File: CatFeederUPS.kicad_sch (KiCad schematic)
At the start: 18 parts, among them J1 JST-PH-2, J2 FEEDER-OUT, U2 BQ24079RGT, U3 TPS61235PRWLR

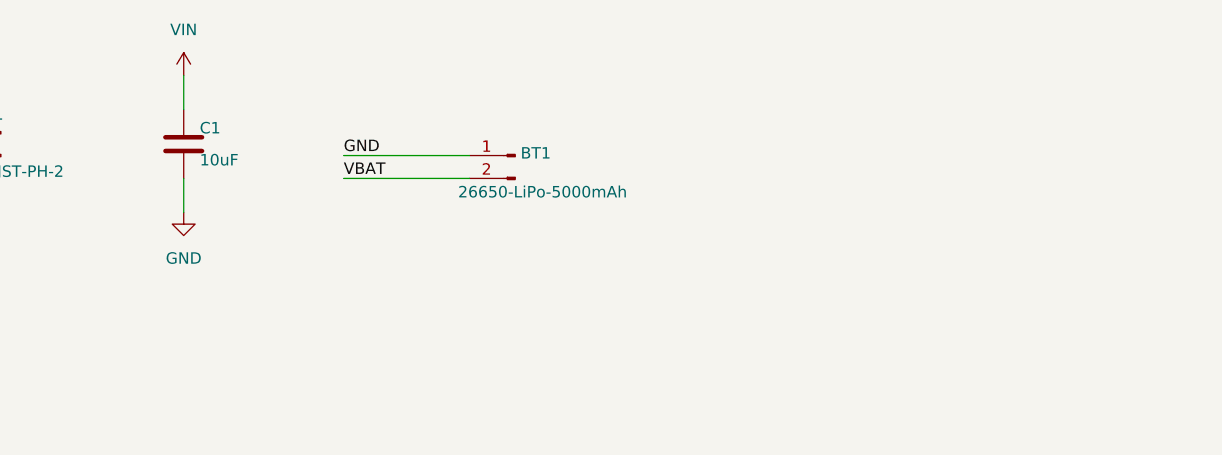
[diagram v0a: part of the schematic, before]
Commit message: Basic layout done, but...
There are a lot of problems with the TPW21635P footprint. It's got a
gigantic  pad 2 (SW) that's a weird T-shape, and both the SnapEDA and
Ultra Librarian footprints represent this as a "polygon" overlaid over
a "pad", which causes DRC to complain bitterly about both electrical
overlap and soldermask overlap, which I cannot fix with board setup,
design rules exceptions etc. etc.

So I had to resort to editing the footprint: I selected the pad, clicked
"edit pad  as geometry shapes" or something in the right-click context
menu, selected both the pad and the polygon, and hit ctrl-e, then saved
it back to the library.

This has fixed the DRC complaints, hopefully I haven't banjaxed it...
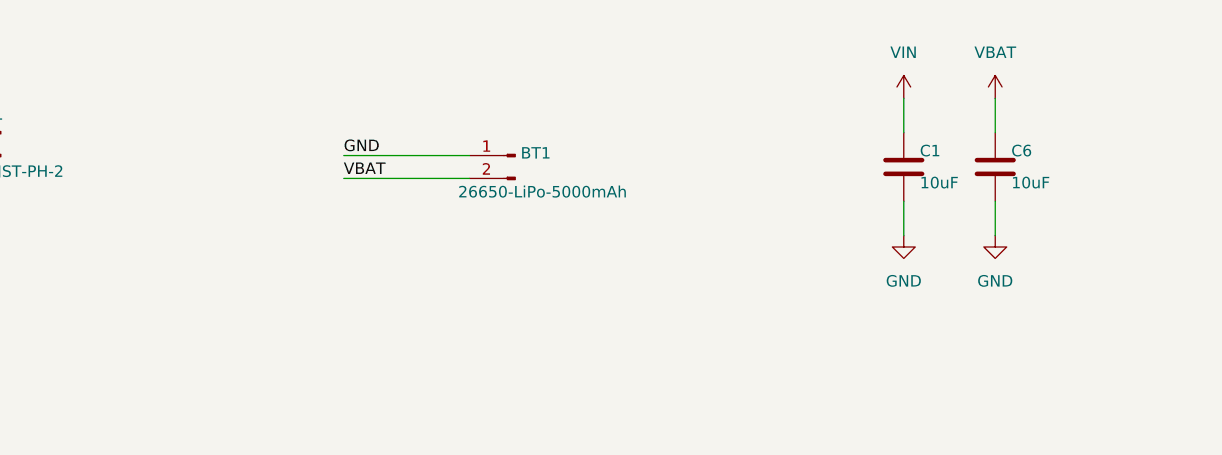
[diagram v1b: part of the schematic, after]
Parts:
- added C6: 10uF, Capacitor_SMD:C_0402_1005Metric, symbol Device:C
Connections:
- net GND: now also C6.2
- net VBAT: now also C6.1
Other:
- moved on the sheet: C1

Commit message: fix LCSC part numbers, and the goddam TPS61235 footprint **again**
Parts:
- BT1, J2: now left out of the parts list
- D2: LCSC C2286 -> C12624
- J1: LCSC C173752 -> (none); now left out of the parts list
- L1: LCSC C408536 -> C695604
- R4, R6: LCSC C11702 -> C114759
- R5: LCSC C11702 -> C60490
- R7: LCSC C11702 -> C3016052
- R8: LCSC C11702 -> C453521
- U2: LCSC (none) -> C140287
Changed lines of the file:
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@@
 			)
 		)
-		(property "LCSC" "C11702"
+		(property "LCSC" "C114759"
 			(at 119.38 105.41 0)
 			(hide yes)
@@
 		(body_style 1)
 		(exclude_from_sim no)
-		(in_bom yes)
+		(in_bom no)
 		(on_board yes)
 		(in_pos_files yes)
@@
 			)
 		)
-		(property "LCSC" "C173752"
-			(at 41.91 43.18 0)
-			(hide yes)
-			(show_name no)
-			(do_not_autoplace no)
-			(effects
-				(font
-					(size 1.27 1.27)
-				)
-			)
-		)
 		(pin "2"
 		)
@@
 			)
 		)
+		(property "LCSC" "C140287"
+			(at 57.15 107.95 0)
+			(hide yes)
+			(show_name no)
+			(do_not_autoplace no)
+			(effects
+				(font
+					(size 1.27 1.27)
+				)
+			)
+		)
 		(pin "8"
 		)
@@
 			)
 		)
-		(property "LCSC" "C11702"
+		(property "LCSC" "C60490"
 			(at 92.71 124.46 0)
 			(hide yes)
@@
 		(body_style 1)
 		(exclude_from_sim no)
-		(in_bom yes)
+		(in_bom no)
 		(on_board yes)
 		(in_pos_files yes)
@@
 			)
 		)
-		(property "LCSC" "C408536"
+		(property "LCSC" "C695604"
 			(at 194.31 83.82 0)
 			(hide yes)
@@
 		(body_style 1)
 		(exclude_from_sim no)
-		(in_bom yes)
+		(in_bom no)
 		(on_board yes)
 		(in_pos_files yes)
@@
 			)
 		)
-		(property "LCSC" "C11702"
+		(property "LCSC" "C3016052"
 			(at 29.21 121.92 0)
 			(hide yes)
@@
 			)
 		)
-		(property "LCSC" "C11702"
+		(property "LCSC" "C114759"
 			(at 104.14 105.41 0)
 			(hide yes)
@@
 			)
 		)
-		(property "LCSC" "C2286"
+		(property "LCSC" "C12624"
 			(at 119.38 93.98 0)
 			(hide yes)
@@
 			)
 		)
-		(property "LCSC" "C11702"
+		(property "LCSC" "C453521"
 			(at 40.64 121.92 0)
 			(hide yes)

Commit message: a couple more component swaps, and away into production we go!
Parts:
- D1: LCSC C2286 -> C130719
- D2: LCSC C12624 -> C74338
- R8: LCSC C453521 -> C67014
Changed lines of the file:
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@@
 			)
 		)
-		(property "LCSC" "C2286"
+		(property "LCSC" "C130719"
 			(at 104.14 93.98 0)
 			(hide yes)
@@
 			)
 		)
-		(property "LCSC" "C12624"
+		(property "LCSC" "C74338"
 			(at 119.38 93.98 0)
 			(hide yes)
@@
 			)
 		)
-		(property "LCSC" "C453521"
+		(property "LCSC" "C67014"
 			(at 40.64 121.92 0)
 			(hide yes)
